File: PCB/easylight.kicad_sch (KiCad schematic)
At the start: 49 parts, among them J1 LiPo (3.7V), J2 USB/PWR, J3 LEDs, J4 AVR-ISP, J8 SW4+, Q1 AO3415_C181094, Q2 AO3415_C181094, SW0 SPEF110100, SW1 TS-1187A-B-A-B, SW2 TS-1187A-B-A-B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

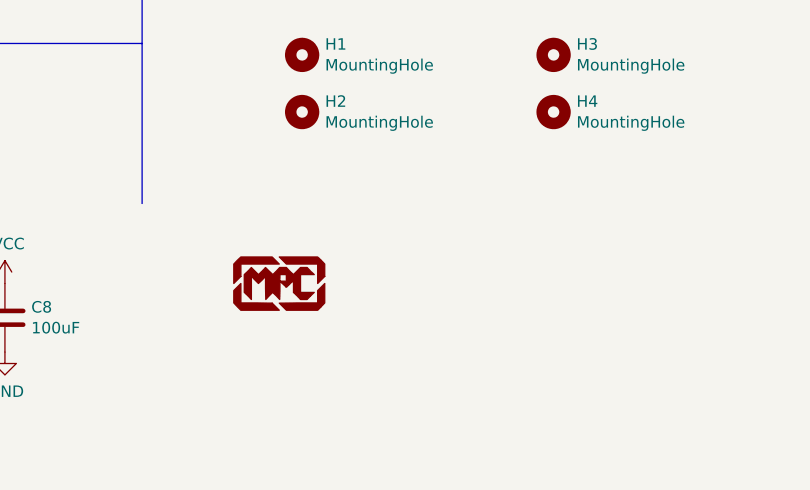
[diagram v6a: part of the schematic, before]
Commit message: improve fills, add qr code, improve silkscreen labels
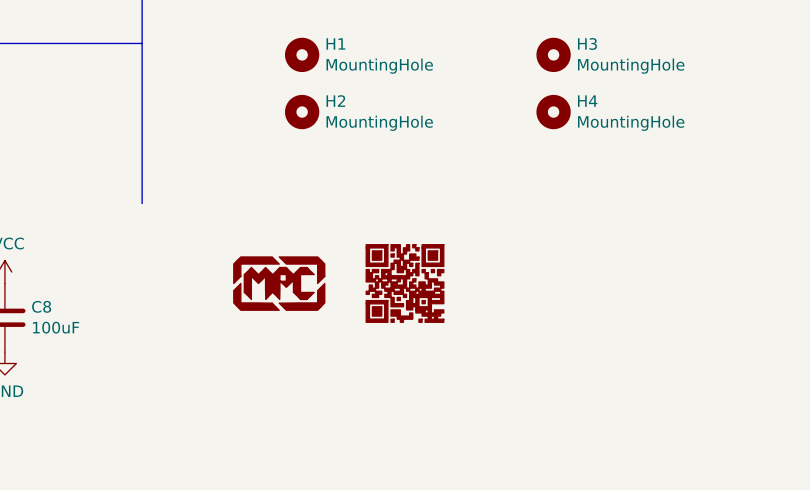
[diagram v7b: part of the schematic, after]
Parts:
- added G2: LOGO, ModischFabrications:MF_QR_7mm, symbol ModischFabrications:LOGO
- L1: footprint ModischFabrications:mpc_logo_10mm -> ModischFabrications:mpc_logo_5mm
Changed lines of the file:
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@@
   (title_block
     (title "EasyLight")
-    (date "2023-02-09")
-    (rev "1.1.2")
+    (date "2023-02-10")
+    (rev "1.2")
     (company "MPC")
   )
@@
       (effects (font (size 1.524 1.524)) hide)
     )
-    (property "Footprint" "ModischFabrications:mpc_logo_10mm" (id 2) (at 193.04 173.99 0)
+    (property "Footprint" "ModischFabrications:mpc_logo_5mm" (id 2) (at 193.04 173.99 0)
       (effects (font (size 1.27 1.27)) hide)
     )
@@
     )
   )
+  (symbol (lib_id "ModischFabrications:LOGO") (at 207.01 173.99 0) (unit 1)
+    (in_bom yes) (on_board yes) (fields_autoplaced)
+    (property "Reference" "G2" (id 0) (at 207.01 169.6243 0)
+      (effects (font (size 1.27 1.27)) hide)
+    )
+    (property "Value" "LOGO" (id 1) (at 207.01 178.3557 0)
+      (effects (font (size 1.27 1.27)) hide)
+    )
+    (property "Footprint" "ModischFabrications:MF_QR_7mm" (id 2) (at 207.01 173.99 0)
+      (effects (font (size 1.27 1.27)) hide)
+    )
+    (property "Datasheet" "" (id 3) (at 207.01 173.99 0)
+      (effects (font (size 1.27 1.27)) hide)
+    )
+  )
   (sheet_instances
     (path "/" (page "1"))
@@
       (reference "G1") (unit 1) (value "LOGO") (footprint "Symbol:WEEE-Logo_4.2x6mm_SilkScreen")
     )
+    (path "/f8302d50-3e5c-4ada-a86c-051f16615ca7"
+      (reference "G2") (unit 1) (value "LOGO") (footprint "ModischFabrications:MF_QR_7mm")
+    )
     (path "/00000000-0000-0000-0000-000063b4b95e"
       (reference "H1") (unit 1) (value "MountingHole") (footprint "ModischFabrications:MountingHole_3.2mm_M3_Pad_Via_NC")
@@
     )
     (path "/00000000-0000-0000-0000-000063d47dd3"
-      (reference "L1") (unit 1) (value "LOGO") (footprint "ModischFabrications:mpc_logo_10mm")
+      (reference "L1") (unit 1) (value "LOGO") (footprint "ModischFabrications:mpc_logo_5mm")
     )
     (path "/a6c2de32-ddcf-434f-8765-93ca2b5b7fc2"
